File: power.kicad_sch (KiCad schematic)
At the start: 15 parts, among them U3 AP62250Z6

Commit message: Updated schematics
Added the input current sense, expansion header and various test points.
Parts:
- added D4: LED, symbol Device:LED
- added R28: 1K, symbol Device:R_Small_US
- added TP17, TP20: TestPoint, symbol Connector:TestPoint
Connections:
- net 3v3: now also R28.1
- net Encoder_VCC: now also TP17.1
- net GND: now also D4.1 (K), TP20.1
- new net: D4.2 (A), R28.2

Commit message: Added RPI stuff
Added power passives and usb passives
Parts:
- FB1: now not fitted
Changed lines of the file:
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@@
 		(in_bom yes)
 		(on_board yes)
-		(dnp no)
+		(dnp yes)
 		(property "Reference" "FB1"
 			(at 71.882 176.53 90)

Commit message: Updated sheet to sheet pinout
Updated pinouts and cleared ERCs
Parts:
- added R50: 0, symbol Device:R_Small_US
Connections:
- net GND: now also R50.2; no longer C17.2, FL1.3, TP20.1
- new net Encoder_GND: C17.2, FL1.3, R50.1, TP20.1
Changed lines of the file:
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@@
 	(paper "A4")
+	(junction
+		(at 52.07 185.42)
+		(diameter 0)
+		(color 0 0 0 0)
+	)
 	(junction
 		(at 60.96 175.26)
@@
 	)
 	(junction
-		(at 52.07 185.42)
-		(diameter 0)
-		(color 0 0 0 0)
-	)
-	(junction
 		(at 36.83 185.42)
 		(diameter 0)
@@
 	(wire
 		(pts
-			(xy 36.83 185.42) (xy 52.07 185.42)
-		)
-		(stroke
-			(width 0)
-			(type default)
-		)
-	)
-	(wire
-		(pts
 			(xy 48.26 49.53) (xy 48.26 52.07)
 		)
@@
 	(wire
 		(pts
+			(xy 46.99 185.42) (xy 52.07 185.42)
+		)
+		(stroke
+			(width 0)
+			(type default)
+		)
+	)
+	(wire
+		(pts
 			(xy 95.25 52.07) (xy 96.52 52.07)
 		)
@@
 		(pts
 			(xy 114.3 49.53) (xy 130.81 49.53)
+		)
+		(stroke
+			(width 0)
+			(type default)
+		)
+	)
+	(wire
+		(pts
+			(xy 36.83 185.42) (xy 41.91 185.42)
 		)
 		(stroke
@@
 	)
 	(symbol
+		(lib_name "GND_3")
 		(lib_id "power:GND")
 		(at 118.11 68.58 0)
@@
 			)
 		)
-		(property "Description" ""
+		(property "Description" "Power symbol creates a global label with name \"GND\" , ground"
 			(at 118.11 68.58 0)
 			(effects
@@
 			)
 		)
-		(property "Description" ""
+		(property "Description" "Power symbol creates a global label with name \"GND\" , ground"
 			(at 48.26 60.96 0)
 			(effects
@@
 	)
 	(symbol
+		(lib_name "GND_5")
 		(lib_id "power:GND")
 		(at 78.74 60.96 0)
@@
 			)
 		)
-		(property "Description" ""
+		(property "Description" "Power symbol creates a global label with name \"GND\" , ground"
 			(at 78.74 60.96 0)
 			(effects
@@
 	)
 	(symbol
+		(lib_name "GND_4")
 		(lib_id "power:GND")
 		(at 106.68 68.58 0)
@@
 			)
 		)
-		(property "Description" ""
+		(property "Description" "Power symbol creates a global label with name \"GND\" , ground"
 			(at 106.68 68.58 0)
 			(effects
@@
 	)
 	(symbol
+		(lib_id "Device:R_Small_US")
+		(at 44.45 185.42 270)
+		(unit 1)
+		(exclude_from_sim no)
+		(in_bom yes)
+		(on_board yes)
+		(dnp yes)
+		(property "Reference" "R50"
+			(at 42.418 187.452 90)
+			(effects
+				(font
+					(size 1.27 1.27)
+				)
+			)
+		)
+		(property "Value" "0"
+			(at 46.99 187.706 90)
+			(effects
+				(font
+					(size 1.27 1.27)
+				)
+			)
+		)
+		(property "Footprint" ""
+			(at 44.45 185.42 0)
+			(effects
+				(font
+					(size 1.27 1.27)
+				)
+				(hide yes)
+			)
+		)
+		(property "Datasheet" "~"
+			(at 44.45 185.42 0)
+			(effects
+				(font
+					(size 1.27 1.27)
+				)
+				(hide yes)
+			)
+		)
+		(property "Description" "Resistor, small US symbol"
+			(at 44.45 185.42 0)
+			(effects
+				(font
+					(size 1.27 1.27)
+				)
+				(hide yes)
+			)
+		)
+		(pin "1"
+		)
+		(pin "2"
+		)
+		(instances
+			(project "moon_child"
+				(path "/9fe08eae-9310-46cf-b272-eac4209a7b3e/7b173924-1b78-4f9c-a21f-8ffedecf02bf"
+					(reference "R50")
+					(unit 1)
+				)
+			)
+		)
+	)
+	(symbol
+		(lib_name "GND_2")
 		(lib_id "power:GND")
 		(at 130.81 68.58 0)
@@
 			)
 		)
-		(property "Description" ""
+		(property "Description" "Power symbol creates a global label with name \"GND\" , ground"
 			(at 130.81 68.58 0)
 			(effects

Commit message: started layout
Preliminary footprint selection
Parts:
- C17, C18: footprint (none) -> Capacitor_SMD:C_0603_1608Metric_Pad1.08x0.95mm_HandSolder
- D4: footprint (none) -> Diode_SMD:D_0603_1608Metric_Pad1.05x0.95mm_HandSolder
- FB1: footprint (none) -> Inductor_SMD:L_2512_6332Metric
- R16, R28, R50: footprint (none) -> Resistor_SMD:R_0603_1608Metric
- TP17, TP20: footprint (none) -> TestPoint:TestPoint_Pad_1.0x1.0mm
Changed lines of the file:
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@@
 			)
 		)
-		(property "Footprint" ""
+		(property "Footprint" "Capacitor_SMD:C_0603_1608Metric_Pad1.08x0.95mm_HandSolder"
 			(at 55.88 180.34 0)
 			(effects
@@
 			)
 		)
-		(property "Footprint" ""
+		(property "Footprint" "Resistor_SMD:R_0603_1608Metric"
 			(at 68.58 170.18 0)
 			(effects
@@
 			)
 		)
-		(property "Footprint" ""
+		(property "Footprint" "TestPoint:TestPoint_Pad_1.0x1.0mm"
 			(at 85.09 173.99 0)
 			(effects
@@
 			)
 		)
-		(property "Footprint" ""
+		(property "Footprint" "Capacitor_SMD:C_0603_1608Metric_Pad1.08x0.95mm_HandSolder"
 			(at 29.21 180.34 0)
 			(effects
@@
 			)
 		)
-		(property "Footprint" ""
+		(property "Footprint" "Resistor_SMD:R_0603_1608Metric"
 			(at 130.81 54.61 0)
 			(effects
@@
 			)
 		)
-		(property "Footprint" ""
+		(property "Footprint" "Diode_SMD:D_0603_1608Metric_Pad1.05x0.95mm_HandSolder"
 			(at 130.81 63.5 0)
 			(effects
@@
 			)
 		)
-		(property "Footprint" ""
+		(property "Footprint" "Resistor_SMD:R_0603_1608Metric"
 			(at 44.45 185.42 0)
 			(effects
@@
 			)
 		)
-		(property "Footprint" ""
+		(property "Footprint" "Inductor_SMD:L_2512_6332Metric"
 			(at 68.58 177.038 90)
 			(effects
@@
 			)
 		)
-		(property "Footprint" ""
+		(property "Footprint" "TestPoint:TestPoint_Pad_1.0x1.0mm"
 			(at 85.09 184.15 0)
 			(effects

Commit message: footprint cleanup
switched to 0402 resistors, updated connectors, etc...
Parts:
- R16, R28, R50: footprint Resistor_SMD:R_0603_1608Metric -> Resistor_SMD:R_0402_1005Metric
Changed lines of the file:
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@@
 			)
 		)
-		(property "Footprint" "Resistor_SMD:R_0603_1608Metric"
+		(property "Footprint" "Resistor_SMD:R_0402_1005Metric"
 			(at 68.58 170.18 0)
 			(effects
@@
 			)
 		)
-		(property "Footprint" "Resistor_SMD:R_0603_1608Metric"
+		(property "Footprint" "Resistor_SMD:R_0402_1005Metric"
 			(at 130.81 54.61 0)
 			(effects
@@
 			)
 		)
-		(property "Footprint" "Resistor_SMD:R_0603_1608Metric"
+		(property "Footprint" "Resistor_SMD:R_0402_1005Metric"
 			(at 44.45 185.42 0)
 			(effects

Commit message: Added USB C Connector
Added usb C connector, consolidated ESD parts, cleaned up footprint selection.
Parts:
- added D10: LED, Diode_SMD:D_0603_1608Metric_Pad1.05x0.95mm_HandSolder, symbol Device:LED
- added D8: D, Diode_SMD:D_SMA, symbol Device:D
- added R54: 3K, Resistor_SMD:R_0402_1005Metric, symbol Device:R_Small_US
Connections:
- net Board_VBATT: now also D8.1 (K)
- net GND: now also D10.1 (K)
- new net: D10.2 (A), R54.2
- new net USB_VBUS: D8.2 (A), R54.1

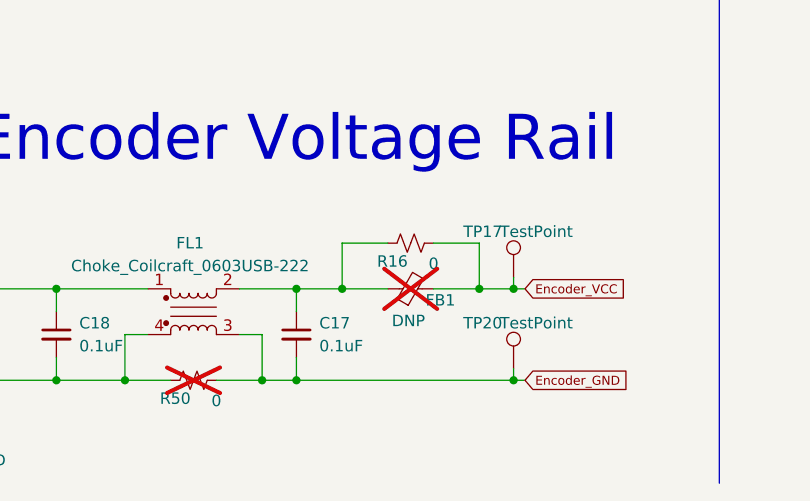
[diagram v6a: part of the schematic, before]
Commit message: layout updates
Updated encoder, esd and other layouts
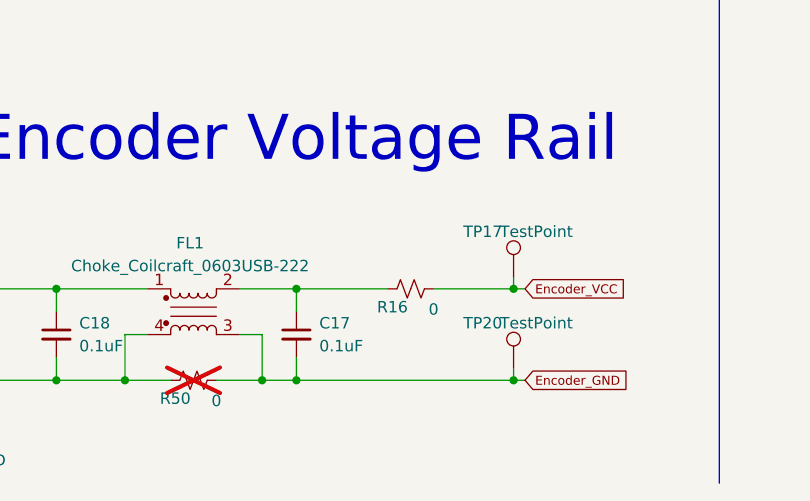
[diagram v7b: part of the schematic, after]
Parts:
- removed FB1: DNP, Inductor_SMD:L_2512_6332Metric, symbol Device:FerriteBead_Small
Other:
- moved on the sheet: R16
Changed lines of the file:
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@@
-	)
-	(junction
-		(at 60.96 175.26)
-		(diameter 0)
-		(color 0 0 0 0)
 	)
 	(junction
@@
 	)
 	(junction
-		(at 76.2 175.26)
-		(diameter 0)
-		(color 0 0 0 0)
-	)
-	(junction
 		(at 114.3 49.53)
 		(diameter 0)
@@
 	(wire
 		(pts
-			(xy 55.88 175.26) (xy 60.96 175.26)
+			(xy 55.88 175.26) (xy 66.04 175.26)
 		)
 		(stroke
@@
 	(wire
 		(pts
-			(xy 60.96 175.26) (xy 66.04 175.26)
-		)
-		(stroke
-			(width 0)
-			(type default)
-		)
-	)
-	(wire
-		(pts
 			(xy 29.21 175.26) (xy 29.21 177.8)
 		)
@@
 	(wire
 		(pts
-			(xy 60.96 170.18) (xy 60.96 175.26)
-		)
-		(stroke
-			(width 0)
-			(type default)
-		)
-	)
-	(wire
-		(pts
 			(xy 121.92 64.77) (xy 121.92 67.31)
 		)
@@
 	(wire
 		(pts
-			(xy 71.12 175.26) (xy 76.2 175.26)
-		)
-		(stroke
-			(width 0)
-			(type default)
-		)
-	)
-	(wire
-		(pts
 			(xy 29.21 185.42) (xy 36.83 185.42)
 		)
@@
 	(wire
 		(pts
-			(xy 76.2 175.26) (xy 80.01 175.26)
-		)
-		(stroke
-			(width 0)
-			(type default)
-		)
-	)
-	(wire
-		(pts
 			(xy 29.21 49.53) (xy 39.37 49.53)
 		)
@@
 	(wire
 		(pts
-			(xy 76.2 170.18) (xy 76.2 175.26)
-		)
-		(stroke
-			(width 0)
-			(type default)
-		)
-	)
-	(wire
-		(pts
 			(xy 57.15 49.53) (xy 68.58 49.53)
 		)
@@
 	(wire
 		(pts
-			(xy 71.12 170.18) (xy 76.2 170.18)
+			(xy 71.12 175.26) (xy 80.01 175.26)
 		)
 		(stroke
@@
 		(pts
 			(xy 102.87 49.53) (xy 106.68 49.53)
-		)
-		(stroke
-			(width 0)
-			(type default)
-		)
-	)
-	(wire
-		(pts
-			(xy 66.04 170.18) (xy 60.96 170.18)
 		)
 		(stroke
@@
 	(symbol
 		(lib_id "Device:R_Small_US")
-		(at 68.58 170.18 270)
+		(at 68.58 175.26 270)
 		(unit 1)
 		(exclude_from_sim no)
@@
 		(dnp no)
 		(property "Reference" "R16"
-			(at 66.548 172.212 90)
+			(at 66.548 177.292 90)
 			(effects
 				(font
@@
 		)
 		(property "Value" "0"
-			(at 71.12 172.466 90)
+			(at 71.12 177.546 90)
 			(effects
 				(font
@@
 		)
 		(property "Footprint" "Resistor_SMD:R_0402_1005Metric"
-			(at 68.58 170.18 0)
+			(at 68.58 175.26 0)
 			(effects
 				(font
@@
 		)
 		(property "Datasheet" "~"
-			(at 68.58 170.18 0)
+			(at 68.58 175.26 0)
 			(effects
 				(font
@@
 		)
 		(property "Description" "Resistor, small US symbol"
-			(at 68.58 170.18 0)
+			(at 68.58 175.26 0)
 			(effects
 				(font
@@
 					(unit 1)
 				)
-			)
-		)
-	)
-	(symbol
-		(lib_id "Device:FerriteBead_Small")
-		(at 68.58 175.26 90)
-		(unit 1)
-		(exclude_from_sim no)
-		(in_bom yes)
-		(on_board yes)
-		(dnp yes)
-		(property "Reference" "FB1"
-			(at 71.882 176.53 90)
-			(effects
-				(font
-					(size 1.27 1.27)
-				)
-			)
-		)
-		(property "Value" "DNP"
-			(at 68.326 178.816 90)
-			(effects
-				(font
-					(size 1.27 1.27)
-				)
-			)
-		)
-		(property "Footprint" "Inductor_SMD:L_2512_6332Metric"
-			(at 68.58 177.038 90)
-			(effects
-				(font
-					(size 1.27 1.27)
-				)
-				(hide yes)
-			)
-		)
-		(property "Datasheet" "~"
-			(at 68.58 175.26 0)
-			(effects
-				(font
-					(size 1.27 1.27)
-				)
-				(hide yes)
-			)
-		)
-		(property "Description" "Ferrite bead, small symbol"
-			(at 68.58 175.26 0)
-			(effects
-				(font
-					(size 1.27 1.27)
-				)
-				(hide yes)
-			)
-		)
-		(pin "2"
-		)
-		(pin "1"
-		)
-		(instances
-			(project ""
-				(path "/9fe08eae-9310-46cf-b272-eac4209a7b3e/7b173924-1b78-4f9c-a21f-8ffedecf02bf"
-					(reference "FB1")
-					(unit 1)
-				)

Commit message: Layout updates
testpoints, usb power, etc.
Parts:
- TP17, TP20: footprint TestPoint:TestPoint_Pad_1.0x1.0mm -> TestPoint:TestPoint_Pad_D1.0mm
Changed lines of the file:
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@@
 			)
 		)
-		(property "Footprint" "TestPoint:TestPoint_Pad_1.0x1.0mm"
+		(property "Footprint" "TestPoint:TestPoint_Pad_D1.0mm"
 			(at 85.09 173.99 0)
 			(effects
@@
 			)
 		)
-		(property "Footprint" "TestPoint:TestPoint_Pad_1.0x1.0mm"
+		(property "Footprint" "TestPoint:TestPoint_Pad_D1.0mm"
 			(at 85.09 184.15 0)
 			(effects
